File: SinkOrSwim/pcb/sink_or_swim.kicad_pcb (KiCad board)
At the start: 2 copper layers, 42.7 x 61.4 mm, 25 parts, among them P101 CONN_01X02, P102 CONN_01X03, P103 CONN_01X02, P201 CONN_01X01, P202 B4_FET, P203 AFTR_FET, Q201 BUK9575-100A, U201 LMV358, U401 LM2931

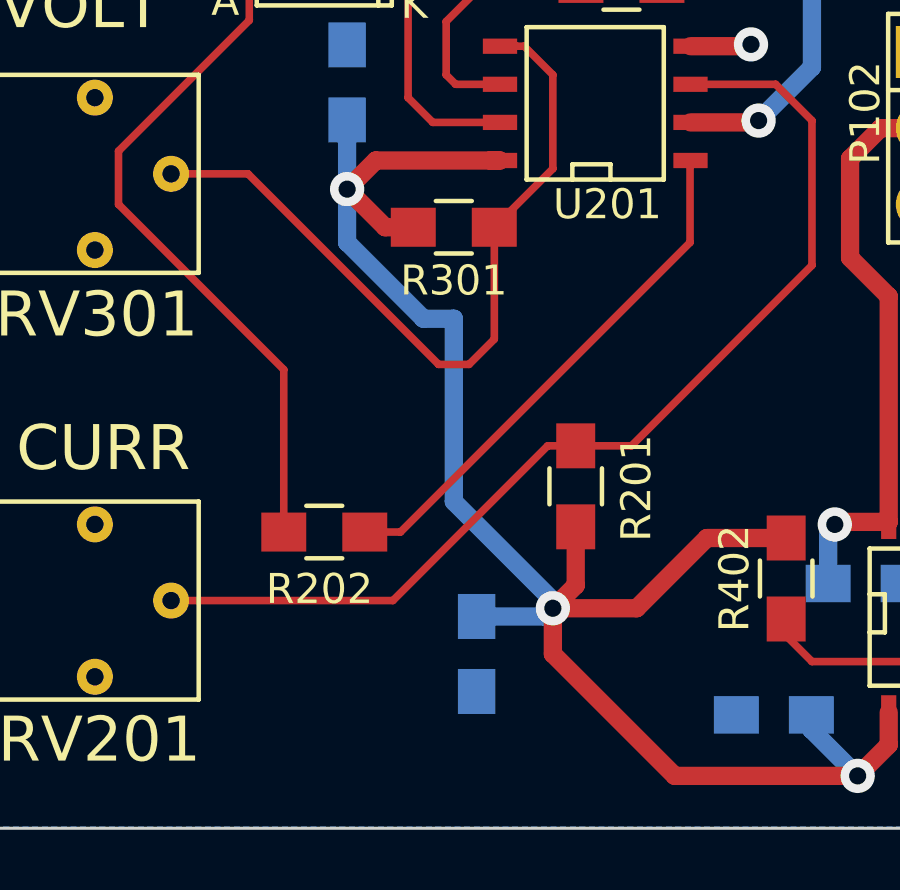
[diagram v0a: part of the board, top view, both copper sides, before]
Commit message: Chart of input voltage vs amps.  Also started getting ready for v2 changes.
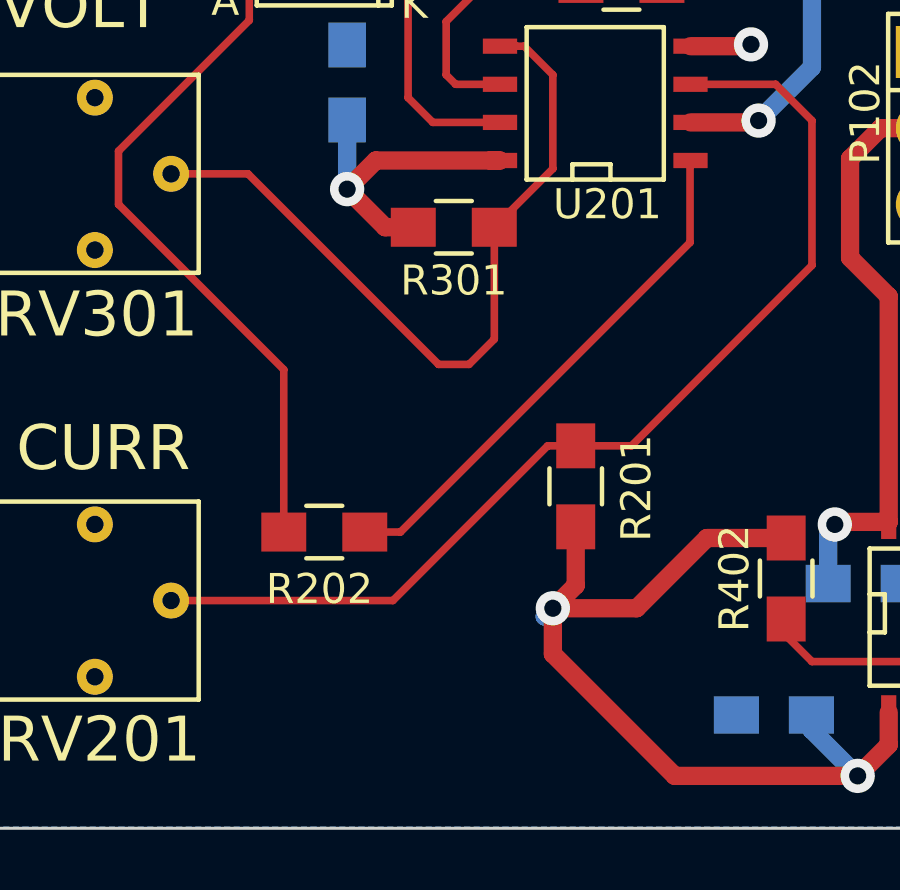
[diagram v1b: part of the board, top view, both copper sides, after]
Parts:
- removed C201: C, Capacitors_SMD:C_0805_HandSoldering
- C301, C401, C402: value C -> .1uf
- P101, P103: value CONN_01X02 -> TERMINAL_BLOCK
- P201: value CONN_01X01 -> HEATSINK
- R401: value R -> 0
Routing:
- net 2.7V: track 61.7 -> 42.0 mm
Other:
- board text added: "SinkOrSwim : csos_v2"
- board text added: "brooke.t.hedrick@gmail.com"
- board text removed: "SinkOrSwim : csos_v1"
- board text removed: "brooke.t.hedick@gmail.com"
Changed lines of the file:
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@@
 (kicad_pcb (version 4) (host pcbnew "(2015-01-29 BZR 5396)-product")
   (general
-    (links 49)
-    (no_connects 1)
-    (area 148.031429 67.513999 200.548 129.050001)
+    (links 47)
+    (no_connects 2)
+    (area 148.031429 67.513999 202.762287 129.050001)
     (thickness 1.6)
     (drawings 14)
-    (tracks 141)
+    (tracks 134)
     (zones 0)
-    (modules 25)
+    (modules 24)
     (nets 16)
   )
@@
   )
   (module Capacitors_SMD:C_0805_HandSoldering (layer B.Cu)
-    (at 165.608 123.19 270)
-    (descr "Capacitor SMD 0805, hand soldering")
-    (tags "capacitor 0805")
-    (attr smd)
-    (fp_text reference C201 (at 0.06 1.84 270) (layer B.SilkS)
-      (effects (font (size 1 1) (thickness 0.15)) (justify mirror))
-    )
-    (fp_text value C (at 0 -2.1 270) (layer B.SilkS) hide
-      (effects (font (size 1 1) (thickness 0.15)) (justify mirror))
-    )
-    (fp_line (start -2.3 1) (end 2.3 1) (layer B.CrtYd) (width 0.05))
-    (fp_line (start -2.3 -1) (end 2.3 -1) (layer B.CrtYd) (width 0.05))
-    (fp_line (start -2.3 1) (end -2.3 -1) (layer B.CrtYd) (width 0.05))
-    (fp_line (start 2.3 1) (end 2.3 -1) (layer B.CrtYd) (width 0.05))
-    (fp_line (start 0.5 0.85) (end -0.5 0.85) (layer B.SilkS) (width 0.15))
-    (fp_line (start -0.5 -0.85) (end 0.5 -0.85) (layer B.SilkS) (width 0.15))
-    (pad 1 smd rect (at -1.25 0 270) (size 1.5 1.25) (layers B.Cu B.Paste B.Mask)
-      (net 1 2.7V))
-    (pad 2 smd rect (at 1.25 0 270) (size 1.5 1.25) (layers B.Cu B.Paste B.Mask)
-      (net 2 GND))
-    (model Capacitors_SMD/C_0805_HandSoldering.wrl
-      (at (xyz 0 0 0))
-      (scale (xyz 1 1 1))
-      (rotate (xyz 0 0 0))
-    )
-  )
-  (module Capacitors_SMD:C_0805_HandSoldering (layer B.Cu)
     (at 161.29 104.14 90)
     (descr "Capacitor SMD 0805, hand soldering")
@@
       (effects (font (size 1 1) (thickness 0.15)) (justify mirror))
     )
-    (fp_text value C (at 0 -2.1 90) (layer B.SilkS) hide
+    (fp_text value .1uf (at 0 -2.1 90) (layer B.SilkS) hide
       (effects (font (size 1 1) (thickness 0.15)) (justify mirror))
     )
@@
       (effects (font (size 1 1) (thickness 0.15)) (justify mirror))
     )
-    (fp_text value C (at 0 -2.1) (layer B.SilkS) hide
+    (fp_text value .1uf (at 0 -2.1) (layer B.SilkS) hide
       (effects (font (size 1 1) (thickness 0.15)) (justify mirror))
     )
@@
       (effects (font (size 1 1) (thickness 0.15)) (justify mirror))
     )
-    (fp_text value C (at 0 -2.1 180) (layer B.SilkS) hide
+    (fp_text value .1uf (at 0 -2.1 180) (layer B.SilkS) hide
       (effects (font (size 1 1) (thickness 0.15)) (justify mirror))
     )
@@
       (effects (font (size 1 1) (thickness 0.15)))
     )
-    (fp_text value R (at 0 2.1 270) (layer F.SilkS) hide
+    (fp_text value 0 (at 0 2.1 270) (layer F.SilkS) hide
       (effects (font (size 1 1) (thickness 0.15)))
     )
@@
       (effects (font (size 1.5 1.5) (thickness 0.15)))
     )
-    (fp_text value CONN_01X01 (at 20.78 -18.97) (layer F.Fab) hide
+    (fp_text value HEATSINK (at 20.78 -18.97) (layer F.Fab) hide
       (effects (font (size 1.5 1.5) (thickness 0.15)))
     )
@@
       (effects (font (size 1.5 1.5) (thickness 0.15)))
     )
-    (fp_text value CONN_01X02 (at 0.13 5.72 90) (layer F.Fab) hide
+    (fp_text value TERMINAL_BLOCK (at 0.13 5.72 90) (layer F.Fab) hide
       (effects (font (size 1.5 1.5) (thickness 0.15)))
     )
@@
       (effects (font (size 1.5 1.5) (thickness 0.15)))
     )
-    (fp_text value CONN_01X02 (at 0.13 5.72 90) (layer F.Fab) hide
+    (fp_text value TERMINAL_BLOCK (at 0.13 5.72 90) (layer F.Fab) hide
       (effects (font (size 1.5 1.5) (thickness 0.15)))
     )
@@
     (effects (font (size 1.5 1.5) (thickness 0.3)) (justify left mirror))
   )
-  (gr_text brooke.t.hedick@gmail.com (at 165.1 69.342 180) (layer B.SilkS)
+  (gr_text brooke.t.hedrick@gmail.com (at 165.62 69.3 180) (layer B.SilkS)
     (effects (font (size 1.5 1.5) (thickness 0.3)) (justify mirror))
   )
-  (gr_text "SinkOrSwim : csos_v1" (at 188.722 80.772 90) (layer B.SilkS)
+  (gr_text "SinkOrSwim : csos_v2" (at 188.722 80.772 90) (layer B.SilkS)
     (effects (font (size 1.5 1.5) (thickness 0.3)) (justify mirror))
   )
@@
   (gr_line (start 149.352 67.564) (end 149.352 129) (angle 90) (layer Edge.Cuts) (width 0.1))
   (segment (start 168.91 120.904) (end 168.148 121.666) (width 0.61) (layer F.Cu) (net 1))
-  (via (at 168.148 121.666) (size 1.143) (layers F.Cu B.Cu) (net 1))
-  (segment (start 168.148 121.666) (end 167.874 121.94) (width 0.61) (layer B.Cu) (net 1))
   (segment (start 168.91 118.952) (end 168.91 120.904) (width 0.61) (layer F.Cu) (net 1))
   (segment (start 170.942 121.666) (end 173.283 119.325) (width 0.61) (layer F.Cu) (net 1))
@@
   (segment (start 179.343 125.137) (end 179.343 126.219) (width 0.61) (layer F.Cu) (net 1))
   (segment (start 166.055 106.741) (end 166.385 106.741) (width 0.61) (layer F.Cu) (net 1))
-  (segment (start 167.874 121.94) (end 168.148 121.666) (width 0.61) (layer B.Cu) (net 1))
-  (segment (start 165.608 121.94) (end 167.874 121.94) (width 0.61) (layer B.Cu) (net 1))
   (segment (start 168.148 123.19) (end 172.212 127.254) (width 0.61) (layer F.Cu) (net 1))
   (segment (start 172.212 127.254) (end 178.308 127.254) (width 0.61) (layer F.Cu) (net 1))
   (segment (start 168.148 121.666) (end 168.148 123.19) (width 0.61) (layer F.Cu) (net 1))
-  (segment (start 163.83 112.014) (end 161.29 109.474) (width 0.61) (layer B.Cu) (net 1))
-  (segment (start 161.29 109.474) (end 161.29 107.696) (width 0.61) (layer B.Cu) (net 1))
   (via (at 161.29 107.696) (size 1.143) (layers F.Cu B.Cu) (net 1))
   (segment (start 161.29 107.696) (end 162.245 106.741) (width 0.61) (layer F.Cu) (net 1))
   (segment (start 162.245 106.741) (end 166.385 106.741) (width 0.61) (layer F.Cu) (net 1))
-  (segment (start 168.148 121.666) (end 168.148 121.412) (width 0.61) (layer B.Cu) (net 1))
-  (segment (start 164.846 118.11) (end 164.846 112.014) (width 0.61) (layer B.Cu) (net 1))
-  (segment (start 168.148 121.412) (end 164.846 118.11) (width 0.61) (layer B.Cu) (net 1))
-  (segment (start 164.846 112.014) (end 163.83 112.014) (width 0.61) (layer B.Cu) (net 1))
   (segment (start 161.29 107.696) (end 161.29 105.39) (width 0.61) (layer B.Cu) (net 1))
   (segment (start 162.56 108.966) (end 161.29 107.696) (width 0.61) (layer F.Cu) (net 1))
   (segment (start 163.496 108.966) (end 162.56 108.966) (width 0.61) (layer F.Cu) (net 1))
+  (segment (start 168.148 121.666) (end 167.874 121.94) (width 0.61) (layer B.Cu) (net 1))
+  (via (at 168.148 121.666) (size 1.143) (layers F.Cu B.Cu) (net 1))
+  (segment (start 167.874 121.94) (end 168.148 121.666) (width 0.61) (layer B.Cu) (net 1))
   (segment (start 178.28 94.68) (end 178.28 91.92) (width 0.61) (layer F.Cu) (net 2))
   (segment (start 178.28 94.68) (end 178.28 96.238) (width 0.61) (layer F.Cu) (net 2))

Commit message: csos getting ready to send out for boards
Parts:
- removed P202: B4_FET, Pin_Headers:Pin_Header_Straight_1x02
- removed P203: AFTR_FET, Pin_Headers:Pin_Header_Straight_1x02
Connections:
- Q201 pad S: GND -> Net-(Q201-PadS)
- R203 pad 1: GND -> Net-(Q201-PadS)
- RV201 pad 1: Net-(RV201-Pad1) -> (no net)
- RV301 pad 1: Net-(RV301-Pad1) -> (no net)
- U201 pad 2: GND -> Net-(Q201-PadS)
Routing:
- net Net-(Q201-PadS): track 0.00 -> 27.7 mm, vias 0 -> 2
- net GND: track 47.4 -> 20.8 mm, vias 6 -> 4
- net 2.7V: track 42.0 -> 58.8 mm
- net /CurrentControl/Current_Sink+: track 41.4 -> 42.3 mm
